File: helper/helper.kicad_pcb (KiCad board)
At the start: 2 copper layers, 22.7 x 114.9 mm, 44 parts, among them J1 Conn_02x34_Odd_Even, J2 Conn_01x08_Male

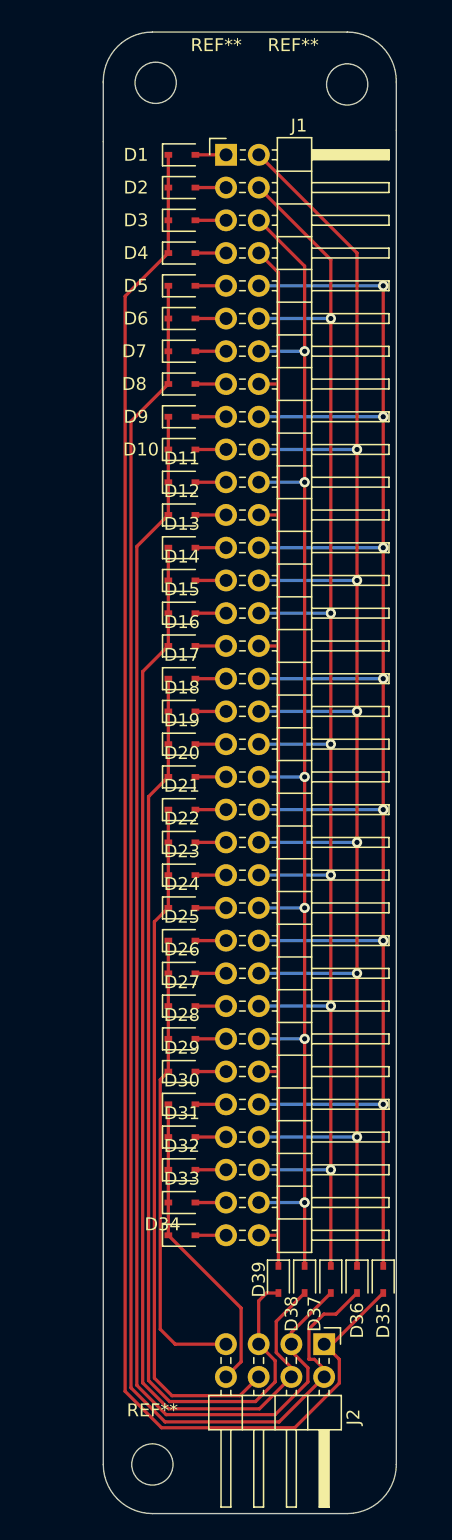
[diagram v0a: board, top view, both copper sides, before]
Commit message: handwire helper for 4/5 x 8 standard matrix with through-hole diodes and ground fill
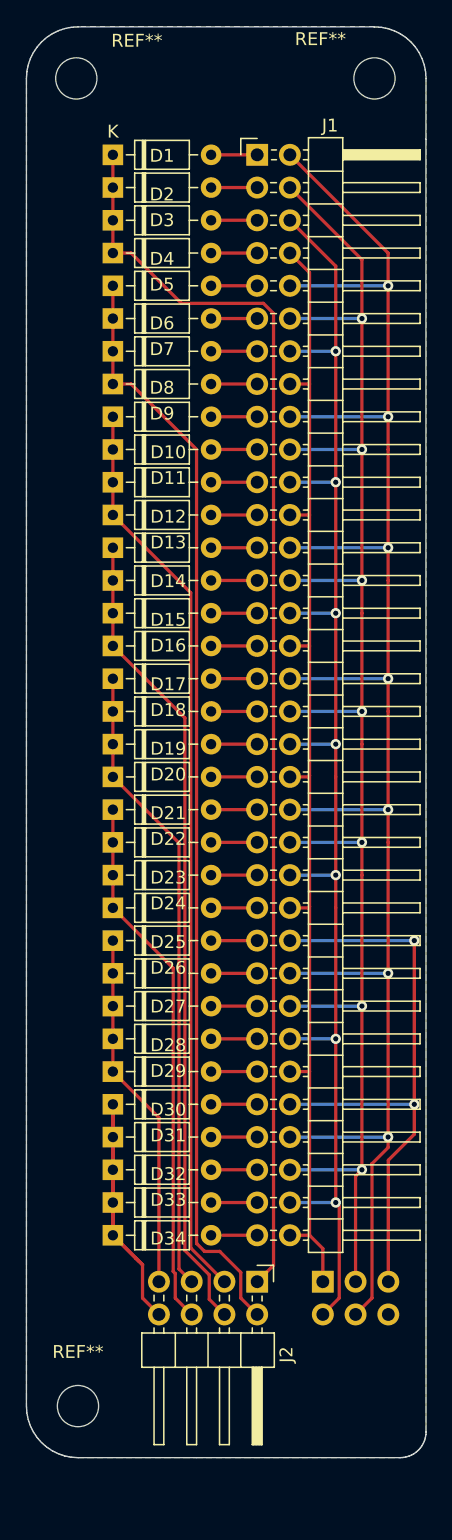
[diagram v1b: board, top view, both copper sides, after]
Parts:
- removed D35, D36, D37, D38, D39: 1N4148WS, Diode_SMD:D_SOD-323
- added J3: Conn_01x06_Male, Connector_PinHeader_2.54mm:PinHeader_2x03_P2.54mm_Horizontal, B.Cu at (94.0, 146.3)
- D1, D10, D11, D12, D13, D14, D15, D16, D17, D18, D19, D2, D20, D21, D22, D23, D24, D25, D26, D27, D28, D29, D3, D30, D31, D32, D33, D34, D4, D5, D6, D7, D8, D9: footprint Diode_SMD:D_SOD-323 -> Diode_THT:D_DO-35_SOD27_P7.62mm_Horizontal
- moved REF** 7.34 mm to (75.0, 156.0)
- moved J2 7.11 mm to (88.9, 146.3)
- moved REF** 6.17 mm to (74.9, 53.0)
- moved D1 5.35 mm to (77.7, 58.9)
- moved D10 5.35 mm to (77.7, 81.8)
- moved D11 5.35 mm to (77.7, 84.3)
- moved D12 5.35 mm to (77.7, 86.9)
- moved D13 5.35 mm to (77.7, 89.4)
- moved D14 5.35 mm to (77.7, 91.9)
- moved D15 5.35 mm to (77.7, 94.5)
- moved D16 5.35 mm to (77.7, 97.0)
- moved D17 5.35 mm to (77.7, 99.6)
- moved D18 5.35 mm to (77.7, 102.1)
- moved D19 5.35 mm to (77.7, 104.6)
- moved D2 5.35 mm to (77.7, 61.5)
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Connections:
- J1 pad 10: Net-(D35-Pad1) -> Net-(J1-Pad2)
- J1 pad 12: Net-(D37-Pad1) -> Net-(J1-Pad12)
- J1 pad 14: Net-(D38-Pad1) -> Net-(J1-Pad14)
- J1 pad 16: Net-(D39-Pad1) -> Net-(J1-Pad16)
- J1 pad 18: Net-(D35-Pad1) -> Net-(J1-Pad2)
- J1 pad 2: Net-(D36-Pad1) -> Net-(J1-Pad2)
- J1 pad 20: Net-(D36-Pad1) -> Net-(J1-Pad12)
- J1 pad 22: Net-(D38-Pad1) -> Net-(J1-Pad14)
- J1 pad 24: Net-(D39-Pad1) -> Net-(J1-Pad16)
- J1 pad 26: Net-(D35-Pad1) -> Net-(J1-Pad2)
- J1 pad 28: Net-(D36-Pad1) -> Net-(J1-Pad12)
- J1 pad 30: Net-(D37-Pad1) -> Net-(J1-Pad14)
- J1 pad 32: Net-(D39-Pad1) -> Net-(J1-Pad16)
- J1 pad 34: Net-(D35-Pad1) -> Net-(J1-Pad2)
- J1 pad 36: Net-(D36-Pad1) -> Net-(J1-Pad12)
- J1 pad 38: Net-(D37-Pad1) -> Net-(J1-Pad14)
- J1 pad 4: Net-(D37-Pad1) -> Net-(J1-Pad12)
- J1 pad 40: Net-(D38-Pad1) -> Net-(J1-Pad16)
- J1 pad 42: Net-(D35-Pad1) -> Net-(J1-Pad2)
- J1 pad 44: Net-(D36-Pad1) -> Net-(J1-Pad12)
- J1 pad 46: Net-(D37-Pad1) -> Net-(J1-Pad14)
- J1 pad 48: Net-(D38-Pad1) -> Net-(J1-Pad16)
- J1 pad 50: Net-(D35-Pad1) -> Net-(J1-Pad50)
- J1 pad 52: Net-(D36-Pad1) -> Net-(J1-Pad2)
- J1 pad 54: Net-(D37-Pad1) -> Net-(J1-Pad12)
- J1 pad 56: Net-(D38-Pad1) -> Net-(J1-Pad14)
- J1 pad 58: Net-(D39-Pad1) -> Net-(J1-Pad16)
- J1 pad 6: Net-(D38-Pad1) -> Net-(J1-Pad14)
- J1 pad 60: Net-(D35-Pad1) -> Net-(J1-Pad50)
- J1 pad 62: Net-(D36-Pad1) -> Net-(J1-Pad2)
- J1 pad 64: Net-(D37-Pad1) -> Net-(J1-Pad12)
- J1 pad 66: Net-(D38-Pad1) -> Net-(J1-Pad14)
- J1 pad 68: Net-(D39-Pad1) -> Net-(J1-Pad16)
- J1 pad 8: Net-(D39-Pad1) -> Net-(J1-Pad16)
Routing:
- net Net-(J1-Pad2): track 0.00 -> 147.5 mm, vias 0 -> 7
- net Net-(D35-Pad1): track 143.6 -> 0.00 mm, vias 7 -> 0
- net Net-(D36-Pad1): track 135.1 -> 0.00 mm, vias 6 -> 0
- net Net-(J1-Pad12): track 0.00 -> 126.5 mm, vias 0 -> 7
- net Net-(D37-Pad1): track 119.5 -> 0.00 mm, vias 6 -> 0
- net Net-(J1-Pad14): track 0.00 -> 111.9 mm, vias 0 -> 7
- net Net-(D38-Pad1): track 103.9 -> 0.00 mm, vias 6 -> 0
- net Net-(J1-Pad16): track 0.00 -> 91.6 mm
- net Net-(D39-Pad1): track 86.8 -> 0.00 mm
- net Net-(J1-Pad50): track 0.00 -> 46.6 mm, vias 0 -> 2
- net Net-(D10-Pad1): track 100.1 -> 70.7 mm
- net Net-(D1-Pad1): track 126.3 -> 97.7 mm
- net Net-(D5-Pad1): track 113.6 -> 86.0 mm
- net Net-(D17-Pad1): track 74.8 -> 49.3 mm
- net Net-(D13-Pad1): track 86.9 -> 63.1 mm
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- added copper zone on B.Cu, net GND
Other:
- board size 22.7 x 114.9 mm -> 31 x 111 mm

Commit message: consolidate row traces so they don't block the fill
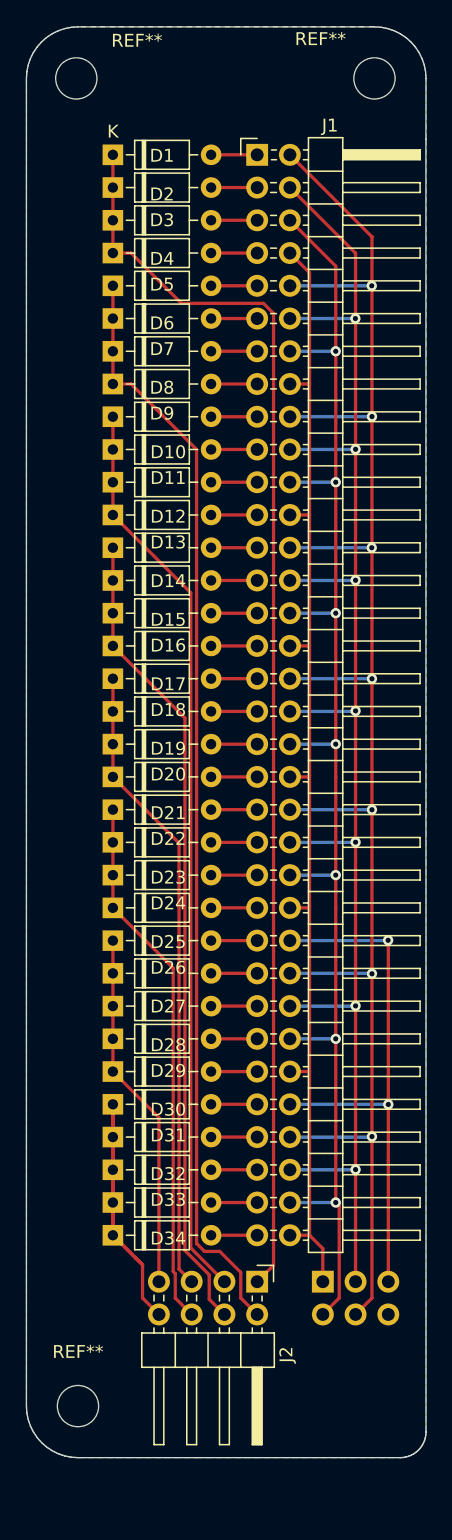
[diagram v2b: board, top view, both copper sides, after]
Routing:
- net Net-(J1-Pad2): track 147.5 -> 137.5 mm
- net Net-(J1-Pad50): track 46.6 -> 41.7 mm
- net Net-(J1-Pad12): track 126.5 -> 122.6 mm

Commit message: Handwire Helper version 0.1 as submitted
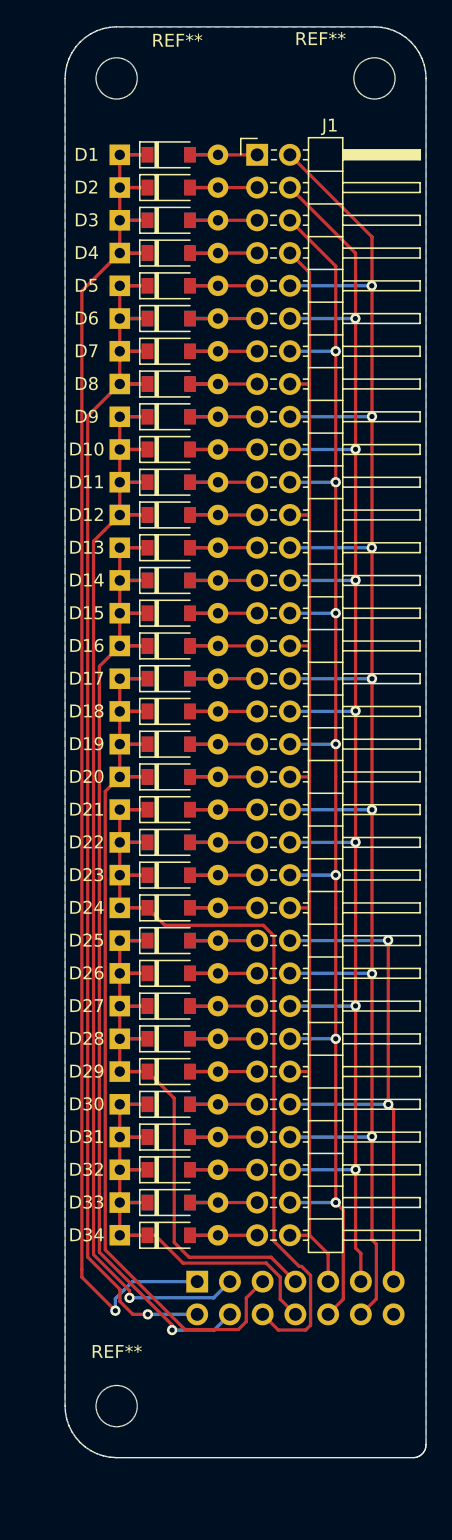
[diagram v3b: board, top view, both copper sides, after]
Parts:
- removed J3: Conn_01x06_Male, Connector_PinHeader_2.54mm:PinHeader_2x03_P2.54mm_Horizontal
- D1, D10, D11, D12, D13, D14, D15, D16, D17, D18, D19, D2, D20, D21, D22, D23, D24, D25, D26, D27, D28, D29, D3, D30, D31, D32, D33, D34, D4, D5, D6, D7, D8, D9: value 1N4148WS -> 1N4148W; footprint Diode_THT:D_DO-35_SOD27_P7.62mm_Horizontal -> handy:Reversable_Diode_SOD-123_THT
- J2: value Conn_01x08_Male -> Conn_01x14_Male; footprint Connector_PinHeader_2.54mm:PinHeader_2x04_P2.54mm_Horizontal -> Connector_PinHeader_2.54mm:PinHeader_2x07_P2.54mm_Horizontal; moved to B.Cu
- moved J2 4.65 mm to (84.2, 146.3)
- moved D1 4.33 mm to (82.0, 58.9)
- moved D10 4.33 mm to (82.0, 81.8)
- moved D11 4.33 mm to (82.0, 84.3)
- moved D12 4.33 mm to (82.0, 86.9)
- moved D13 4.33 mm to (82.0, 89.4)
- moved D14 4.33 mm to (82.0, 91.9)
- moved D15 4.33 mm to (82.0, 94.5)
- moved D16 4.33 mm to (82.0, 97.0)
- moved D17 4.33 mm to (82.0, 99.6)
- moved D18 4.33 mm to (82.0, 102.1)
- moved D19 4.33 mm to (82.0, 104.6)
- moved D2 4.33 mm to (82.0, 61.5)
- moved D20 4.33 mm to (82.0, 107.2)
- moved D21 4.33 mm to (82.0, 109.7)
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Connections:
- J1 pad 10: Net-(J1-Pad2) -> Net-(J1-Pad10)
- J1 pad 18: Net-(J1-Pad2) -> Net-(J1-Pad10)
- J1 pad 2: Net-(J1-Pad2) -> Net-(J1-Pad10)
- J1 pad 26: Net-(J1-Pad2) -> Net-(J1-Pad10)
- J1 pad 34: Net-(J1-Pad2) -> Net-(J1-Pad10)
- J1 pad 42: Net-(J1-Pad2) -> Net-(J1-Pad10)
- J1 pad 52: Net-(J1-Pad2) -> Net-(J1-Pad10)
- J1 pad 62: Net-(J1-Pad2) -> Net-(J1-Pad10)
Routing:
- net Net-(J1-Pad10): track 0.00 -> 137.8 mm, vias 0 -> 7
- net Net-(J1-Pad2): track 137.5 -> 0.00 mm, vias 7 -> 0
- net Net-(D17-Pad1): track 49.3 -> 79.4 mm
- net Net-(D21-Pad1): track 41.7 -> 71.4 mm
- net Net-(D25-Pad1): track 27.9 -> 56.4 mm
- net Net-(D10-Pad1): track 70.7 -> 95.8 mm, vias 0 -> 1
- net Net-(D13-Pad1): track 63.1 -> 85.9 mm, vias 0 -> 1
- net Net-(D1-Pad1): track 97.7 -> 117.0 mm, vias 0 -> 1
- net Net-(D5-Pad1): track 86.0 -> 104.5 mm, vias 0 -> 1
- net Net-(D30-Pad1): track 31.5 -> 46.7 mm
- net Net-(D34-Pad2): track 2.67 -> 7.38 mm
- net Net-(D9-Pad2): track 3.57 -> 7.38 mm
- net Net-(D8-Pad2): track 3.57 -> 7.38 mm
- net Net-(D7-Pad2): track 3.57 -> 7.38 mm
- net Net-(D6-Pad2): track 3.57 -> 7.38 mm
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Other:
- board size 31 x 111 mm -> 28 x 111 mm
